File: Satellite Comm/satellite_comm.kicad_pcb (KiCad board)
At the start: 2 copper layers, 139.7 x 100.3 mm, 10 parts, among them J1 RockBlock Connector, J2 PC104_40Pin_2.54mm-WhitworthS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, U1 SAM-M8Q

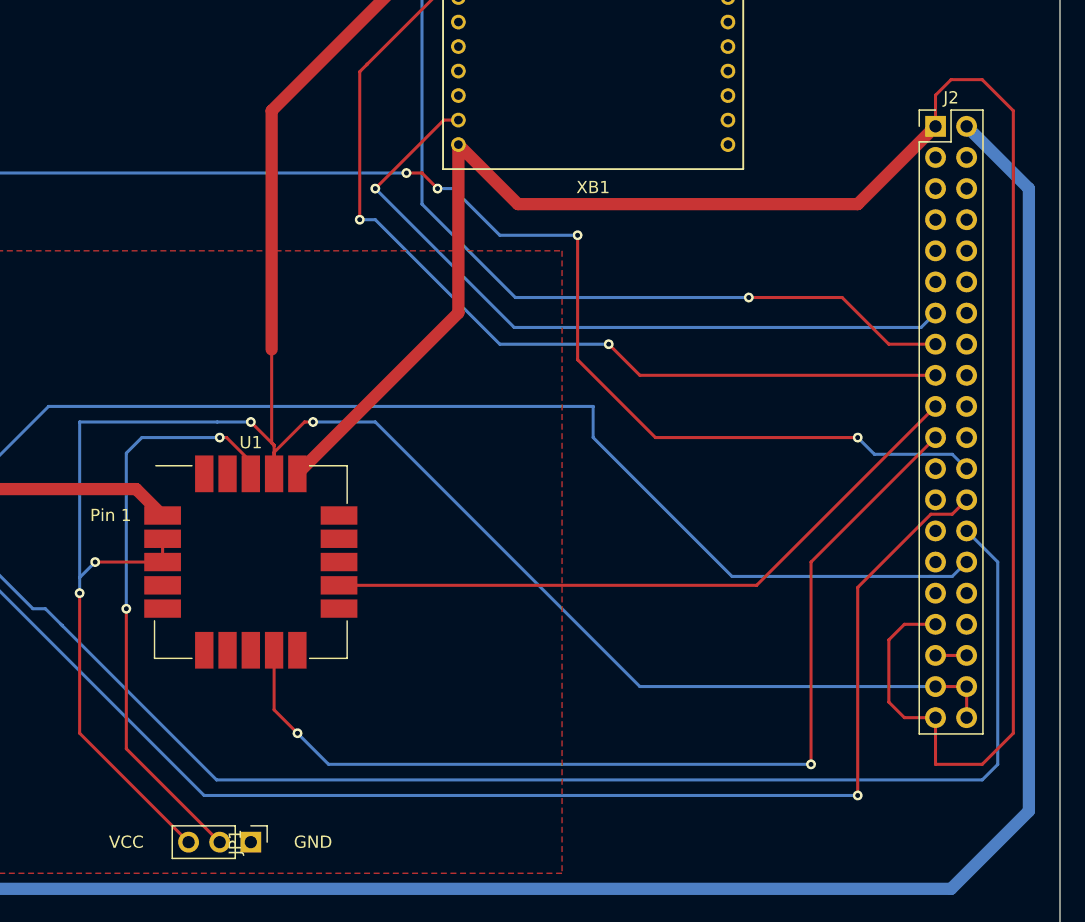
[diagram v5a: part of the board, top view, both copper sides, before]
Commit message: made all ground and power tracks thicker; decreased front copper trails through ground plane
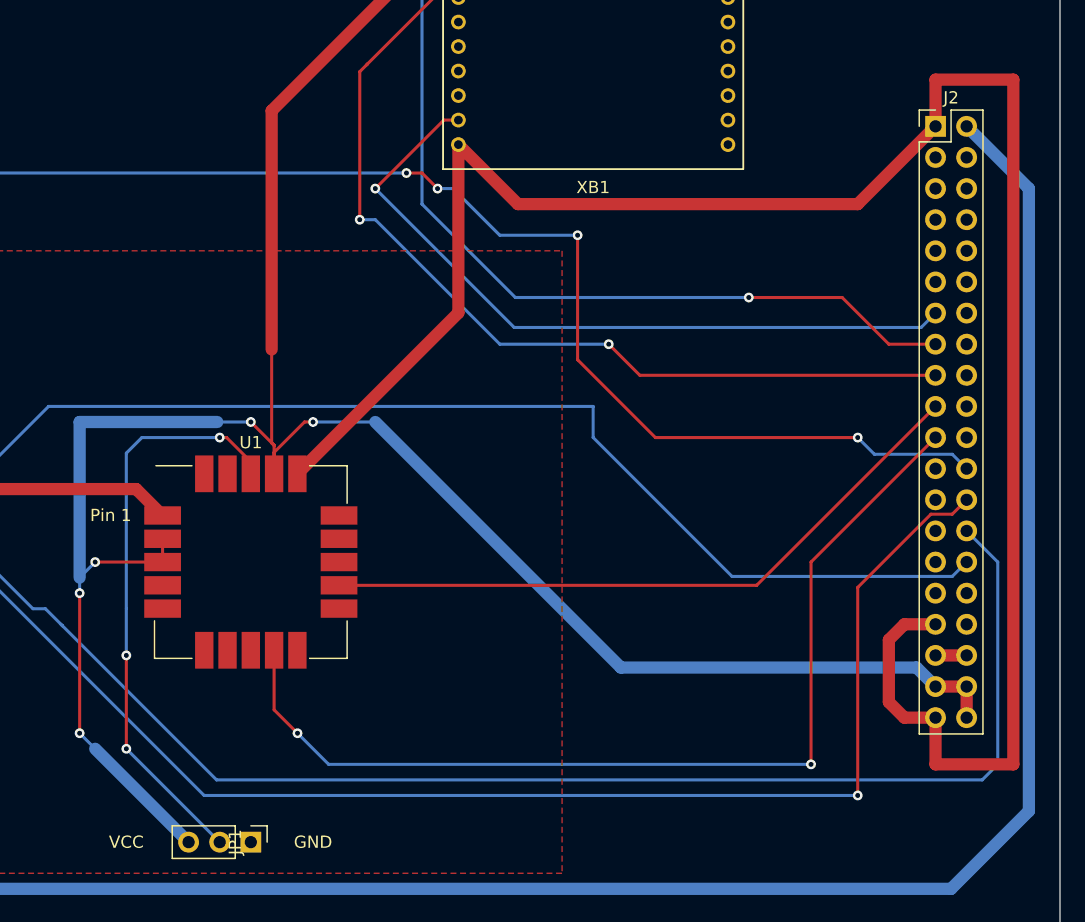
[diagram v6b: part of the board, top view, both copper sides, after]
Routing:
- net GND: track 229.7 -> 233.4 mm
- net Net-(JP1-Pad2): vias 2 -> 3
- net +3V3: vias 4 -> 5
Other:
- board text removed: "placed j2 exactly over old j1 and deleted old j1 because old j1 had all the wrong tracks"
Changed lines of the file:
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@@
   (general
     (thickness 1.6)
-    (drawings 26)
-    (tracks 171)
+    (drawings 25)
+    (tracks 175)
     (zones 0)
     (modules 10)
@@
     )
   )
-  (gr_text "placed j2 exactly over old j1 and deleted old j1 because old j1 had all the wrong tracks" (at 190.5 53.34) (layer Cmts.User)
-    (effects (font (size 1 1) (thickness 0.15)))
-  )
   (gr_text "Pin 1" (at 87.63 83.82) (layer F.SilkS)
     (effects (font (size 1 1) (thickness 0.15)))
@@
   (segment (start 47.86499 81.67501) (end 43.18 86.36) (width 1) (layer F.Cu) (net 1))
   (segment (start 43.18 86.36) (end 34.29 86.36) (width 0.25) (layer F.Cu) (net 1))
-  (segment (start 154.94 52.07) (end 154.94 49.53) (width 0.25) (layer F.Cu) (net 1))
-  (segment (start 154.94 49.53) (end 156.21 48.26) (width 0.25) (layer F.Cu) (net 1))
-  (segment (start 156.21 48.26) (end 158.75 48.26) (width 0.25) (layer F.Cu) (net 1))
-  (segment (start 158.75 48.26) (end 161.29 50.8) (width 0.25) (layer F.Cu) (net 1))
-  (segment (start 161.29 50.8) (end 161.29 101.6) (width 0.25) (layer F.Cu) (net 1))
-  (segment (start 161.29 101.6) (end 158.75 104.14) (width 0.25) (layer F.Cu) (net 1))
-  (segment (start 158.75 104.14) (end 154.94 104.14) (width 0.25) (layer F.Cu) (net 1))
-  (segment (start 154.94 104.14) (end 154.94 100.33) (width 0.25) (layer F.Cu) (net 1))
-  (segment (start 154.94 92.71) (end 152.4 92.71) (width 0.25) (layer F.Cu) (net 1))
-  (segment (start 152.4 92.71) (end 151.13 93.98) (width 0.25) (layer F.Cu) (net 1))
-  (segment (start 151.13 93.98) (end 151.13 99.06) (width 0.25) (layer F.Cu) (net 1))
-  (segment (start 152.4 100.33) (end 154.94 100.33) (width 0.25) (layer F.Cu) (net 1))
-  (segment (start 151.13 99.06) (end 152.4 100.33) (width 0.25) (layer F.Cu) (net 1))
   (segment (start 116 53.56) (end 120.86 58.42) (width 1) (layer F.Cu) (net 1))
   (segment (start 148.59 58.42) (end 154.94 52.07) (width 1) (layer F.Cu) (net 1))
@@
   (segment (start 33.02 82.55) (end 34.855 82.55) (width 0.25) (layer F.Cu) (net 1))
   (segment (start 33.02 85.09) (end 33.02 82.55) (width 0.25) (layer F.Cu) (net 1))
+  (segment (start 154.94 92.71) (end 152.4 92.71) (width 1) (layer F.Cu) (net 1))
+  (segment (start 152.4 92.71) (end 151.13 93.98) (width 1) (layer F.Cu) (net 1))
+  (segment (start 151.13 93.98) (end 151.13 99.06) (width 1) (layer F.Cu) (net 1))
+  (segment (start 151.13 99.06) (end 152.4 100.33) (width 1) (layer F.Cu) (net 1))
+  (segment (start 152.4 100.33) (end 154.94 100.33) (width 1) (layer F.Cu) (net 1))
+  (segment (start 154.94 52.07) (end 154.94 48.26) (width 1) (layer F.Cu) (net 1))
+  (segment (start 154.94 48.26) (end 161.29 48.26) (width 1) (layer F.Cu) (net 1))
+  (segment (start 161.29 48.26) (end 161.29 104.14) (width 1) (layer F.Cu) (net 1))
+  (segment (start 161.29 104.14) (end 154.94 104.14) (width 1) (layer F.Cu) (net 1))
+  (segment (start 154.94 104.14) (end 154.94 100.33) (width 1) (layer F.Cu) (net 1))
   (via (at 41.91 80.01) (size 0.8) (drill 0.4) (layers F.Cu B.Cu) (net 2))
   (segment (start 49.53 87.63) (end 41.91 80.01) (width 0.25) (layer B.Cu) (net 2))
@@
   (segment (start 99.06 76.2) (end 100.96 78.1) (width 0.25) (layer F.Cu) (net 23))
   (segment (start 85.09 88.9) (end 86.36 87.63) (width 0.25) (layer B.Cu) (net 23))
-  (segment (start 85.09 88.9) (end 85.09 76.2) (width 0.25) (layer B.Cu) (net 23))
-  (segment (start 85.09 76.2) (end 96.323002 76.2) (width 0.25) (layer B.Cu) (net 23))
-  (segment (start 154.94 97.79) (end 157.48 97.79) (width 0.25) (layer F.Cu) (net 23) (status 30))
-  (segment (start 154.94 97.79) (end 130.81 97.79) (width 0.25) (layer B.Cu) (net 23))
-  (segment (start 130.81 97.79) (end 109.22 76.2) (width 0.25) (layer B.Cu) (net 23))
   (segment (start 109.22 76.2) (end 104.14 76.2) (width 0.25) (layer B.Cu) (net 23))
-  (segment (start 157.48 97.79) (end 157.48 100.33) (width 0.25) (layer F.Cu) (net 23))
   (segment (start 116 35.56) (end 100.76 50.8) (width 1) (layer F.Cu) (net 23))
   (segment (start 100.76 50.8) (end 100.76 70.28) (width 1) (layer F.Cu) (net 23))
@@
   (segment (start 85.09 90.17) (end 85.09 88.9) (width 0.25) (layer B.Cu) (net 23))
   (via (at 85.09 90.17) (size 0.8) (drill 0.4) (layers F.Cu B.Cu) (net 23))
-  (segment (start 85.09 101.6) (end 93.98 110.49) (width 0.25) (layer F.Cu) (net 23))
   (segment (start 85.09 90.17) (end 85.09 101.6) (width 0.25) (layer F.Cu) (net 23))
-  (segment (start 154.94 95.25) (end 157.48 95.25) (width 0.25) (layer F.Cu) (net 24) (status 30))
+  (segment (start 154.94 97.79) (end 157.48 97.79) (width 1) (layer F.Cu) (net 23))
+  (segment (start 157.48 97.79) (end 157.48 100.33) (width 1) (layer F.Cu) (net 23))
+  (segment (start 153.389999 96.239999) (end 129.259999 96.239999) (width 1) (layer B.Cu) (net 23))
+  (segment (start 154.94 97.79) (end 153.389999 96.239999) (width 1) (layer B.Cu) (net 23))
+  (segment (start 129.259999 96.239999) (end 109.22 76.2) (width 1) (layer B.Cu) (net 23))
+  (segment (start 85.09 101.6) (end 85.09 101.6) (width 0.25) (layer F.Cu) (net 23))
+  (via (at 85.09 101.6) (size 0.8) (drill 0.4) (layers F.Cu B.Cu) (net 23))
+  (segment (start 85.09 76.2) (end 85.09 88.9) (width 1) (layer B.Cu) (net 23))
+  (segment (start 85.09 76.2) (end 96.323002 76.2) (width 1) (layer B.Cu) (net 23))
+  (segment (start 93.98 110.49) (end 86.36 102.87) (width 1) (layer B.Cu) (net 23))
+  (segment (start 86.36 102.87) (end 85.09 101.6) (width 0.25) (layer B.Cu) (net 23))
+  (segment (start 154.94 95.25) (end 157.48 95.25) (width 1) (layer F.Cu) (net 24))
   (via (at 96.52 77.47) (size 0.8) (drill 0.4) (layers F.Cu B.Cu) (net 32))
   (segment (start 99.06 79.444315) (end 99.06 80.43) (width 0.25) (layer F.Cu) (net 32))
@@
   (segment (start 96.52 77.47) (end 90.17 77.47) (width 0.25) (layer B.Cu) (net 32))
   (segment (start 90.17 77.47) (end 88.9 78.74) (width 0.25) (layer B.Cu) (net 32))
-  (via (at 88.9 91.44) (size 0.8) (drill 0.4) (layers F.Cu B.Cu) (net 32))
   (segment (start 88.9 78.74) (end 88.9 91.44) (width 0.25) (layer B.Cu) (net 32))
-  (segment (start 88.9 102.87) (end 96.52 110.49) (width 0.25) (layer F.Cu) (net 32))
-  (segment (start 88.9 91.44) (end 88.9 102.87) (width 0.25) (layer F.Cu) (net 32))
+  (segment (start 88.9 102.87) (end 88.9 102.87) (width 0.25) (layer F.Cu) (net 32))
+  (via (at 88.9 102.87) (size 0.8) (drill 0.4) (layers F.Cu B.Cu) (net 32))
+  (segment (start 88.9 102.87) (end 96.52 110.49) (width 0.25) (layer B.Cu) (net 32))
+  (via (at 88.9 95.25) (size 0.8) (drill 0.4) (layers F.Cu B.Cu) (net 32))
+  (segment (start 88.9 91.44) (end 88.9 95.25) (width 0.25) (layer B.Cu) (net 32))
+  (segment (start 88.9 95.25) (end 88.9 102.87) (width 0.25) (layer F.Cu) (net 32))
   (zone (net 1) (net_name GND) (layer F.Cu) (hatch edge 0.508)
     (connect_pads (clearance 0.508))
